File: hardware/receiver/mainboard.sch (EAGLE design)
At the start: 19 parts, among them J2 POWER_JACKPTH, J3 AVR_SPI_PRG_6PTH, Q1 MOSFET-NCHANNELAO3404A, U1 ATMEGA328P_TQFP, U2 RFM69HCW, U4 RELAY-9007

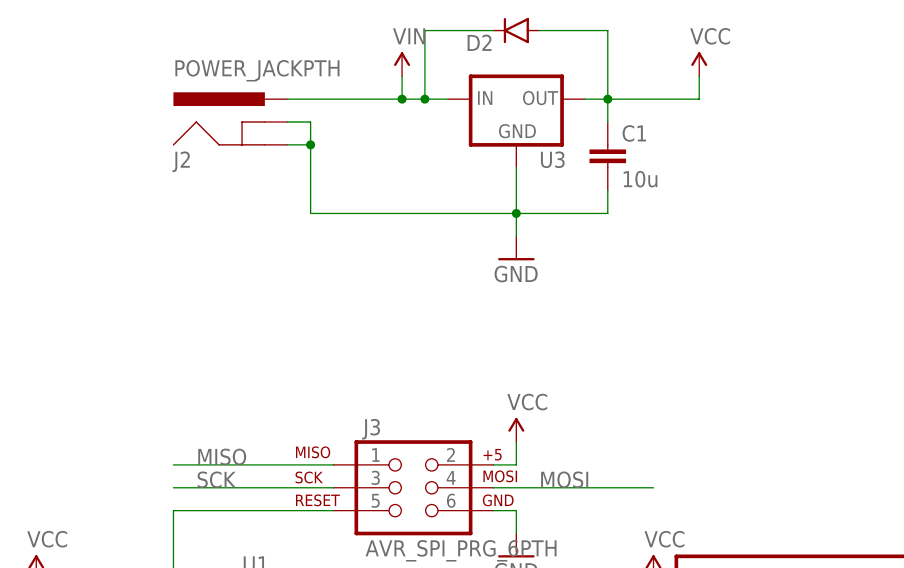
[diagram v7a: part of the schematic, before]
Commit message: Replaced LDO and relay and  updated BOM
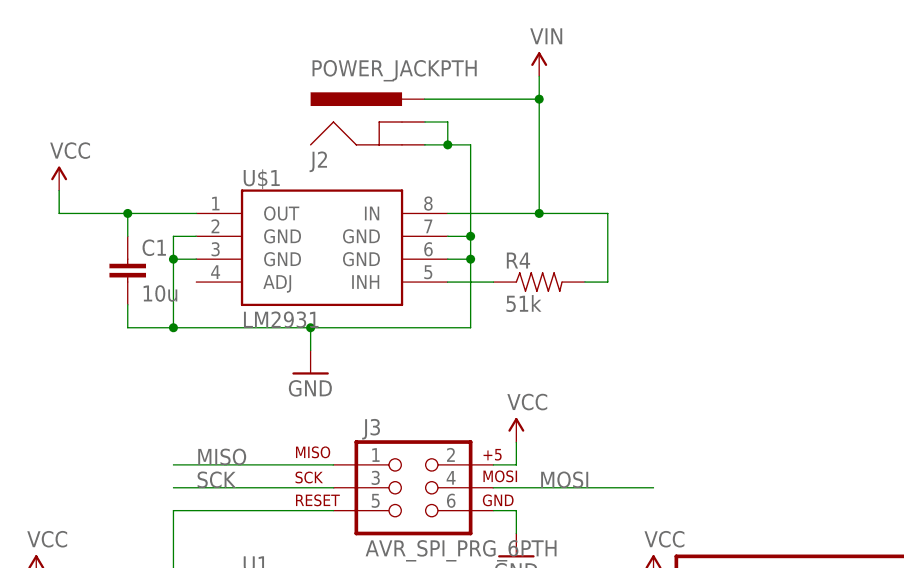
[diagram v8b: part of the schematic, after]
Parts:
- removed D2: (no value), SparkFun-DiscreteSemi:DIODEBAS16
- removed U3: (no value), SparkFun-PowerIC:V_REG_78XXTO-92_UNTESTED
- added R4: 51k, SparkFun-Passives:RESISTOR0603-RES
- added U$1: LM2931, SparkFun-PowerIC:LM2931
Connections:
- new net N$19: R4.1, U$1.INH
- net GND: now also U$1.GND@2, U$1.GND@3, U$1.GND@6, U$1.GND@7; no longer U3.GND
- net VCC: now also U$1.OUT; no longer D2.A, U3.OUT
- net VIN: now also R4.2, U$1.IN; no longer D2.C, U3.IN
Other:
- moved on the sheet: C1, J2
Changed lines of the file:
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@@
 <part name="C4" library="SparkFun-Passives" deviceset="CAP" device="1206" value="10u"/>
 <part name="R3" library="SparkFun-Passives" deviceset="RESISTOR" device="0603-RES" value="47k"/>
-<part name="U3" library="SparkFun-PowerIC" deviceset="V_REG_78XX" device="TO-92_UNTESTED"/>
 <part name="SUPPLY7" library="SparkFun-Aesthetics" deviceset="VIN" device=""/>
 <part name="SUPPLY8" library="SparkFun-Aesthetics" deviceset="VIN" device=""/>
-<part name="D2" library="SparkFun-DiscreteSemi" deviceset="DIODE" device="BAS16"/>
 <part name="SUPPLY5" library="SparkFun-Aesthetics" deviceset="VIN" device=""/>
 <part name="U4" library="Electromechanical" deviceset="RELAY-9007" device=""/>
+<part name="U$1" library="SparkFun-PowerIC" deviceset="LM2931" device=""/>
+<part name="R4" library="SparkFun-Passives" deviceset="RESISTOR" device="0603-RES" value="51k"/>
 </parts>
 <sheets>
@@
 <instance part="U2" gate="G$1" x="180.34" y="43.18"/>
 <instance part="J1" gate="G$1" x="210.82" y="7.62" rot="R180"/>
-<instance part="J2" gate="G$1" x="58.42" y="99.06"/>
-<instance part="C1" gate="G$1" x="96.52" y="99.06"/>
+<instance part="J2" gate="G$1" x="73.66" y="99.06"/>
+<instance part="C1" gate="G$1" x="43.18" y="86.36"/>
 <instance part="C2" gate="G$1" x="33.02" y="33.02"/>
 <instance part="C3" gate="G$1" x="180.34" y="63.5" rot="R90"/>
-<instance part="GND1" gate="1" x="86.36" y="88.9"/>
-<instance part="SUPPLY1" gate="G$1" x="106.68" y="109.22"/>
+<instance part="GND1" gate="1" x="63.5" y="76.2"/>
+<instance part="SUPPLY1" gate="G$1" x="35.56" y="96.52"/>
 <instance part="R1" gate="G$1" x="40.64" y="50.8"/>
 <instance part="SUPPLY2" gate="G$1" x="33.02" y="53.34"/>
@@
 <instance part="C4" gate="G$1" x="149.86" y="-17.78"/>
 <instance part="R3" gate="G$1" x="144.78" y="55.88" rot="R90"/>
-<instance part="U3" gate="G$1" x="86.36" y="106.68"/>
-<instance part="SUPPLY7" gate="G$1" x="73.66" y="109.22"/>
+<instance part="SUPPLY7" gate="G$1" x="88.9" y="109.22"/>
 <instance part="SUPPLY8" gate="G$1" x="167.64" y="15.24"/>
-<instance part="D2" gate="G$1" x="86.36" y="114.3" rot="R180"/>
 <instance part="SUPPLY5" gate="G$1" x="101.6" y="38.1"/>
 <instance part="U4" gate="G$1" x="180.34" y="7.62"/>
+<instance part="U$1" gate="G$1" x="66.04" y="88.9"/>
+<instance part="R4" gate="G$1" x="88.9" y="86.36"/>
 </instances>
 <busses>
@@
 </segment>
 <segment>
-<pinref part="J2" gate="G$1" pin="GNDBREAK"/>
-<wire x1="60.96" y1="104.14" x2="63.5" y2="104.14" width="0.1524" layer="91"/>
-<wire x1="63.5" y1="104.14" x2="63.5" y2="101.6" width="0.1524" layer="91"/>
-<wire x1="63.5" y1="101.6" x2="63.5" y2="93.98" width="0.1524" layer="91"/>
-<pinref part="J2" gate="G$1" pin="GND"/>
-<wire x1="60.96" y1="101.6" x2="63.5" y2="101.6" width="0.1524" layer="91"/>
-<junction x="63.5" y="101.6"/>
-<pinref part="U3" gate="G$1" pin="GND"/>
-<wire x1="63.5" y1="93.98" x2="86.36" y2="93.98" width="0.1524" layer="91"/>
-<wire x1="86.36" y1="93.98" x2="86.36" y2="99.06" width="0.1524" layer="91"/>
-<pinref part="GND1" gate="1" pin="GND"/>
-<wire x1="86.36" y1="91.44" x2="86.36" y2="93.98" width="0.1524" layer="91"/>
-<junction x="86.36" y="93.98"/>
-<pinref part="C1" gate="G$1" pin="2"/>
-<wire x1="96.52" y1="96.52" x2="96.52" y2="93.98" width="0.1524" layer="91"/>
-<wire x1="96.52" y1="93.98" x2="86.36" y2="93.98" width="0.1524" layer="91"/>
-</segment>
-<segment>
 <pinref part="GND6" gate="1" pin="GND"/>
 <wire x1="109.22" y1="35.56" x2="109.22" y2="38.1" width="0.1524" layer="91"/>
@@
 <wire x1="109.22" y1="38.1" x2="111.76" y2="38.1" width="0.1524" layer="91"/>
 <wire x1="111.76" y1="38.1" x2="111.76" y2="45.72" width="0.1524" layer="91"/>
+</segment>
+<segment>
+<pinref part="GND1" gate="1" pin="GND"/>
+<wire x1="63.5" y1="78.74" x2="63.5" y2="81.28" width="0.1524" layer="91"/>
+<pinref part="J2" gate="G$1" pin="GNDBREAK"/>
+<wire x1="76.2" y1="104.14" x2="78.74" y2="104.14" width="0.1524" layer="91"/>
+<wire x1="78.74" y1="104.14" x2="78.74" y2="101.6" width="0.1524" layer="91"/>
+<pinref part="J2" gate="G$1" pin="GND"/>
+<wire x1="78.74" y1="101.6" x2="76.2" y2="101.6" width="0.1524" layer="91"/>
+<pinref part="U$1" gate="G$1" pin="GND@6"/>
+<wire x1="78.74" y1="88.9" x2="81.28" y2="88.9" width="0.1524" layer="91"/>
+<wire x1="81.28" y1="88.9" x2="81.28" y2="91.44" width="0.1524" layer="91"/>
+<wire x1="81.28" y1="91.44" x2="81.28" y2="101.6" width="0.1524" layer="91"/>
+<wire x1="81.28" y1="101.6" x2="78.74" y2="101.6" width="0.1524" layer="91"/>
+<junction x="78.74" y="101.6"/>
+<pinref part="U$1" gate="G$1" pin="GND@7"/>
+<wire x1="78.74" y1="91.44" x2="81.28" y2="91.44" width="0.1524" layer="91"/>
+<junction x="81.28" y="91.44"/>
+<wire x1="63.5" y1="81.28" x2="81.28" y2="81.28" width="0.1524" layer="91"/>
+<wire x1="81.28" y1="81.28" x2="81.28" y2="88.9" width="0.1524" layer="91"/>
+<junction x="81.28" y="88.9"/>
+<pinref part="U$1" gate="G$1" pin="GND@2"/>
+<wire x1="50.8" y1="91.44" x2="48.26" y2="91.44" width="0.1524" layer="91"/>
+<wire x1="48.26" y1="91.44" x2="48.26" y2="88.9" width="0.1524" layer="91"/>
+<wire x1="48.26" y1="88.9" x2="48.26" y2="81.28" width="0.1524" layer="91"/>
+<wire x1="48.26" y1="81.28" x2="63.5" y2="81.28" width="0.1524" layer="91"/>
+<junction x="63.5" y="81.28"/>
+<pinref part="U$1" gate="G$1" pin="GND@3"/>
+<wire x1="50.8" y1="88.9" x2="48.26" y2="88.9" width="0.1524" layer="91"/>
+<junction x="48.26" y="88.9"/>
+<pinref part="C1" gate="G$1" pin="2"/>
+<wire x1="43.18" y1="83.82" x2="43.18" y2="81.28" width="0.1524" layer="91"/>
+<wire x1="43.18" y1="81.28" x2="48.26" y2="81.28" width="0.1524" layer="91"/>
+<junction x="48.26" y="81.28"/>
 </segment>
 </net>
@@
 </segment>
 <segment>
+<pinref part="U$1" gate="G$1" pin="OUT"/>
 <pinref part="SUPPLY1" gate="G$1" pin="VCC"/>
-<wire x1="106.68" y1="109.22" x2="106.68" y2="106.68" width="0.1524" layer="91"/>
-<pinref part="U3" gate="G$1" pin="OUT"/>
-<wire x1="106.68" y1="106.68" x2="96.52" y2="106.68" width="0.1524" layer="91"/>
+<wire x1="50.8" y1="93.98" x2="43.18" y2="93.98" width="0.1524" layer="91"/>
+<wire x1="43.18" y1="93.98" x2="35.56" y2="93.98" width="0.1524" layer="91"/>
+<wire x1="35.56" y1="93.98" x2="35.56" y2="96.52" width="0.1524" layer="91"/>
 <pinref part="C1" gate="G$1" pin="1"/>
-<wire x1="96.52" y1="106.68" x2="93.98" y2="106.68" width="0.1524" layer="91"/>
-<wire x1="96.52" y1="104.14" x2="96.52" y2="106.68" width="0.1524" layer="91"/>
-<junction x="96.52" y="106.68"/>
-<pinref part="D2" gate="G$1" pin="A"/>
-<wire x1="88.9" y1="114.3" x2="96.52" y2="114.3" width="0.1524" layer="91"/>
-<wire x1="96.52" y1="114.3" x2="96.52" y2="106.68" width="0.1524" layer="91"/>
+<wire x1="43.18" y1="91.44" x2="43.18" y2="93.98" width="0.1524" layer="91"/>
+<junction x="43.18" y="93.98"/>
 </segment>
 </net>
@@
 </net>
 <net name="VIN" class="0">
-<segment>
-<pinref part="J2" gate="G$1" pin="PWR"/>
-<wire x1="60.96" y1="106.68" x2="73.66" y2="106.68" width="0.1524" layer="91"/>
-<pinref part="U3" gate="G$1" pin="IN"/>
-<pinref part="SUPPLY7" gate="G$1" pin="VIN"/>
-<wire x1="73.66" y1="106.68" x2="76.2" y2="106.68" width="0.1524" layer="91"/>
-<wire x1="76.2" y1="106.68" x2="78.74" y2="106.68" width="0.1524" layer="91"/>
-<wire x1="73.66" y1="109.22" x2="73.66" y2="106.68" width="0.1524" layer="91"/>
-<junction x="73.66" y="106.68"/>
-<pinref part="D2" gate="G$1" pin="C"/>
-<wire x1="83.82" y1="114.3" x2="76.2" y2="114.3" width="0.1524" layer="91"/>
-<wire x1="76.2" y1="114.3" x2="76.2" y2="106.68" width="0.1524" layer="91"/>
-<junction x="76.2" y="106.68"/>
-</segment>
 <segment>
 <pinref part="D1" gate="G$1" pin="C"/>
@@
 <wire x1="109.22" y1="40.64" x2="109.22" y2="45.72" width="0.1524" layer="91"/>
 </segment>
+<segment>
+<pinref part="J2" gate="G$1" pin="PWR"/>
+<wire x1="76.2" y1="106.68" x2="88.9" y2="106.68" width="0.1524" layer="91"/>
+<wire x1="88.9" y1="106.68" x2="88.9" y2="93.98" width="0.1524" layer="91"/>
+<pinref part="U$1" gate="G$1" pin="IN"/>
+<wire x1="88.9" y1="93.98" x2="78.74" y2="93.98" width="0.1524" layer="91"/>
+<pinref part="SUPPLY7" gate="G$1" pin="VIN"/>
+<wire x1="88.9" y1="109.22" x2="88.9" y2="106.68" width="0.1524" layer="91"/>
+<junction x="88.9" y="106.68"/>
+<pinref part="R4" gate="G$1" pin="2"/>
+<wire x1="93.98" y1="86.36" x2="96.52" y2="86.36" width="0.1524" layer="91"/>
+<wire x1="96.52" y1="86.36" x2="96.52" y2="93.98" width="0.1524" layer="91"/>
+<wire x1="96.52" y1="93.98" x2="88.9" y2="93.98" width="0.1524" layer="91"/>
+<junction x="88.9" y="93.98"/>
+</segment>
 </net>
 <net name="N$9" class="0">
@@
 </segment>
 </net>
+<net name="N$19" class="0">
+<segment>
+<pinref part="R4" gate="G$1" pin="1"/>
+<pinref part="U$1" gate="G$1" pin="INH"/>
+<wire x1="83.82" y1="86.36" x2="78.74" y2="86.36" width="0.1524" layer="91"/>
+</segment>
+</net>
